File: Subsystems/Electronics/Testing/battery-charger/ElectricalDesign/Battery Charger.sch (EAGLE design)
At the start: 117 parts, among them J1 USB4515-GF-A_REVA, J3 10103592-0001LF, Q1 CSD16406Q3, Q2 CSD16406Q3, Q3 DMN2008LFU, Q4 DMN2008LFU, Q5 DMN2008LFU, Q6 BC817, Q7 BC817, SW6 [Override]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

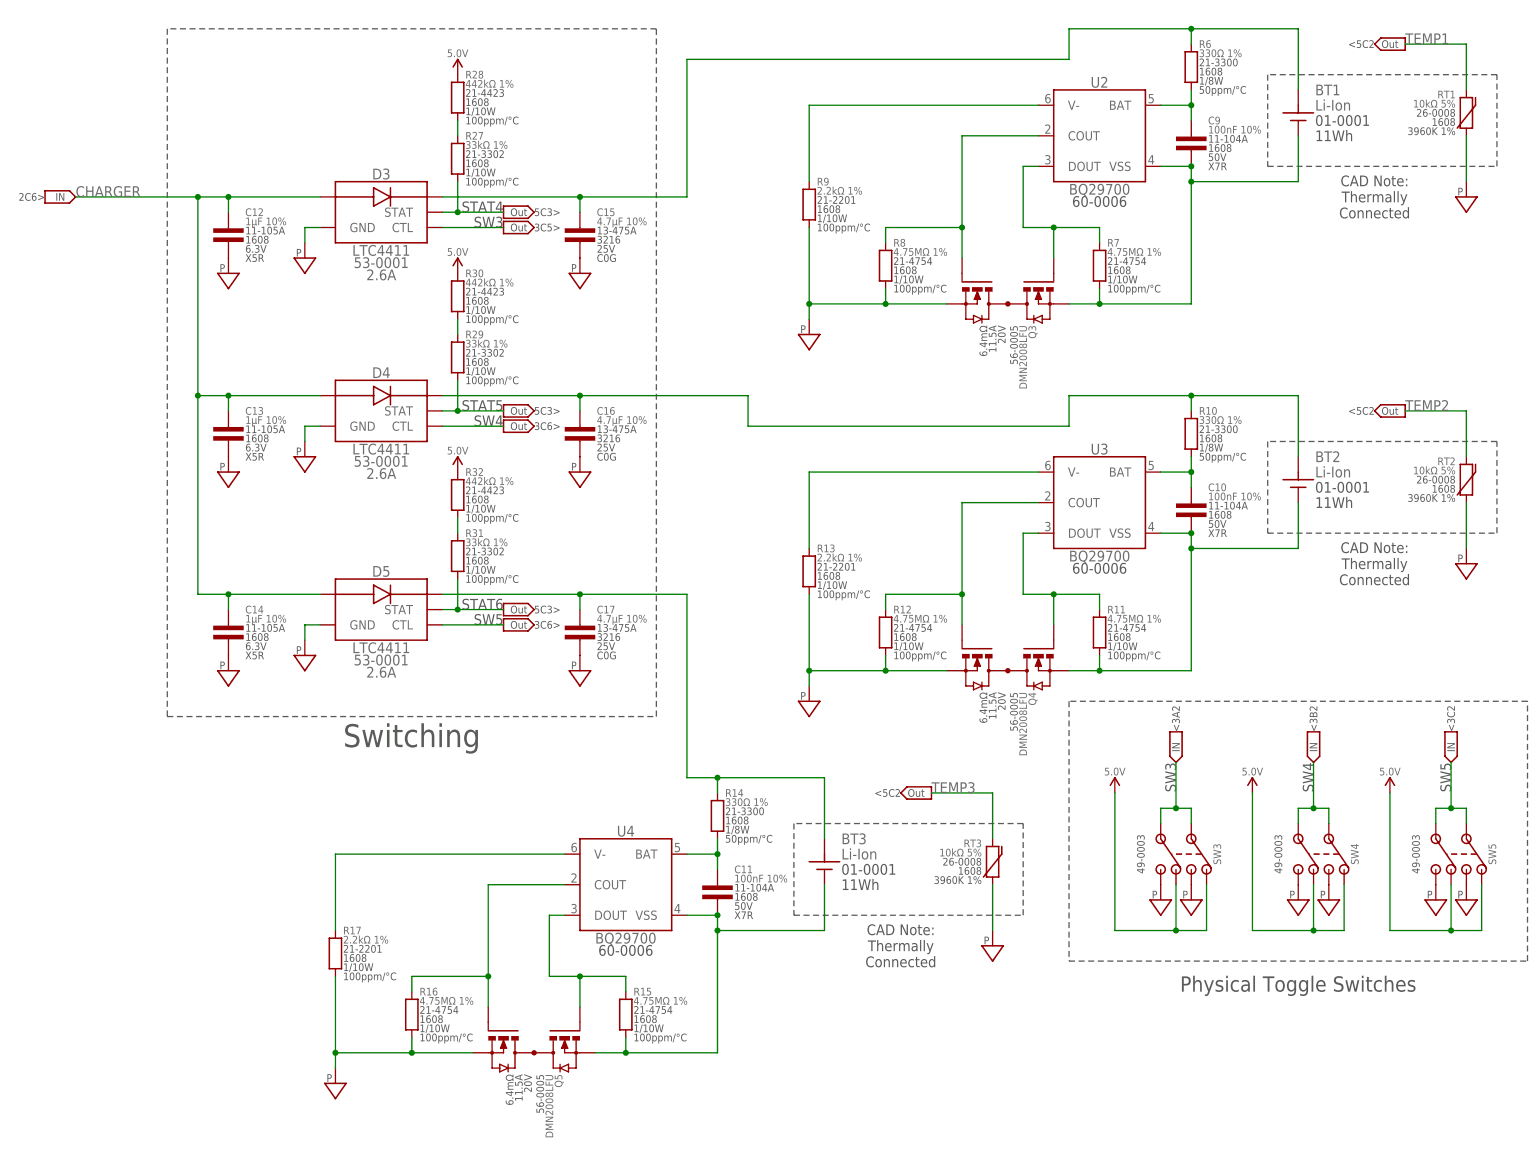
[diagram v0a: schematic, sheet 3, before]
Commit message: Added Test Points
Added test points for the important nets
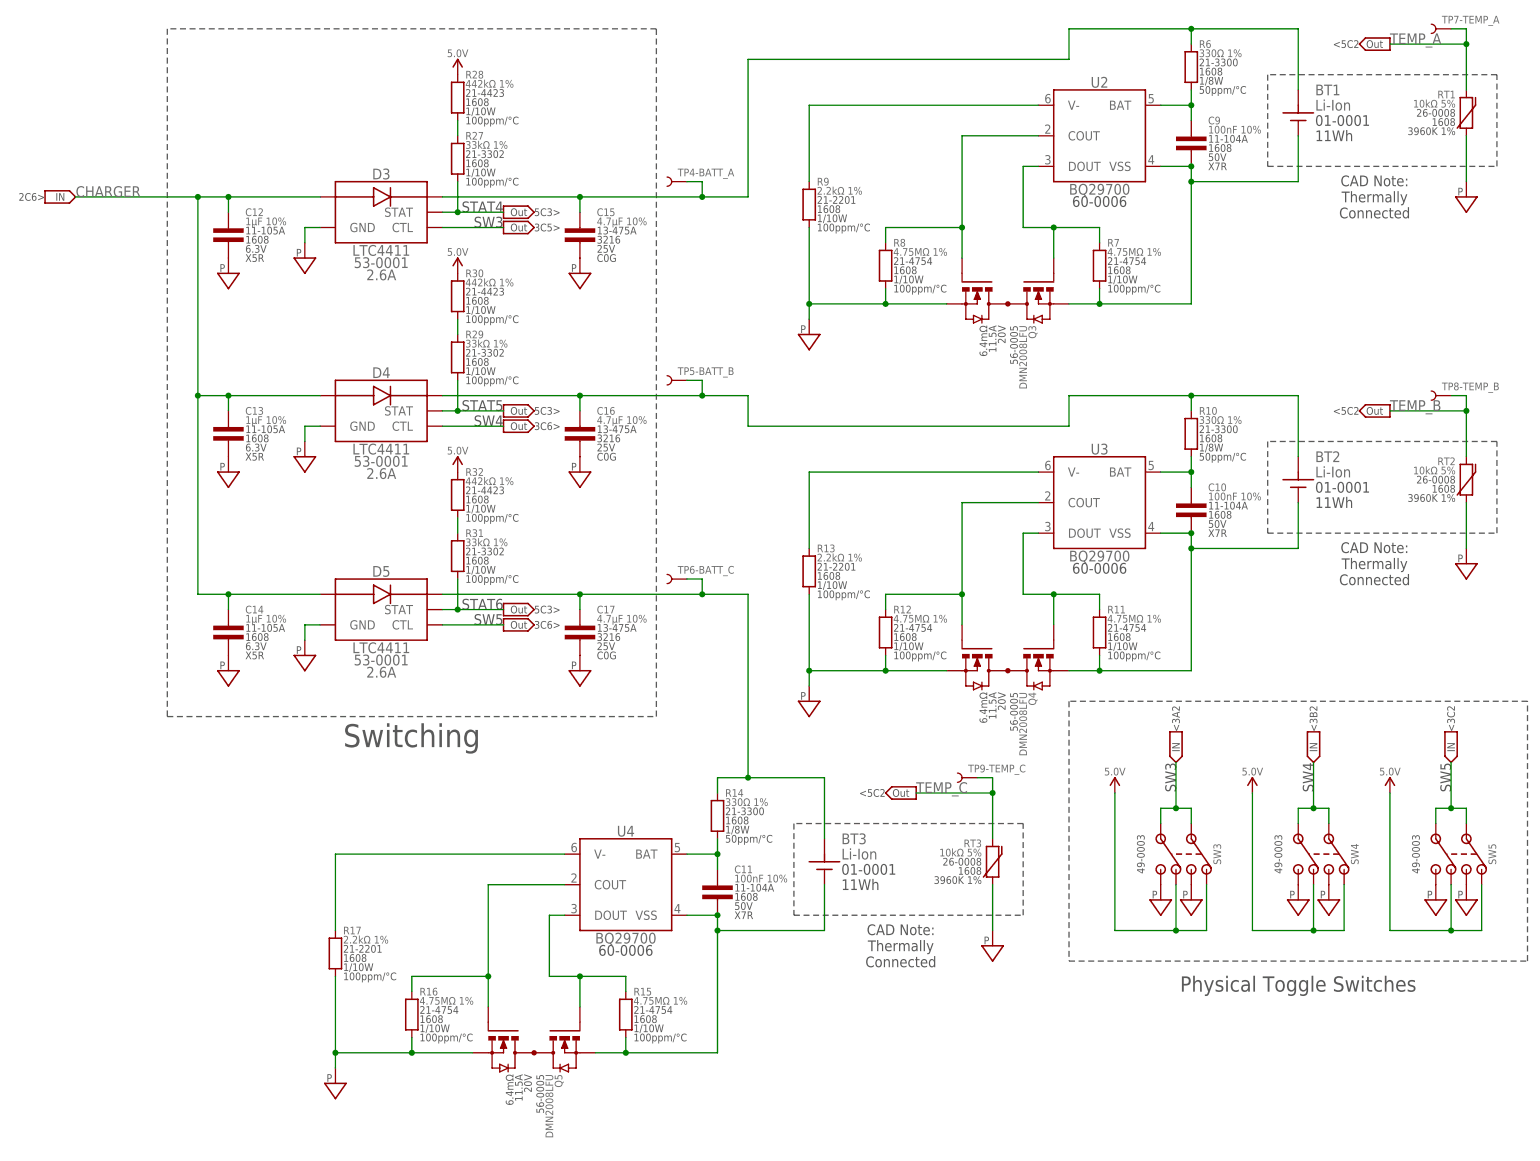
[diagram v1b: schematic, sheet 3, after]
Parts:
- added TP1-5.0V, TP10-USB_5.0V, TP11-CN2102N_VDD, TP12-3.3V, TP2-CHARGER, TP3-TS, TP4-BATT_A, TP5-BATT_B, TP6-BATT_C, TP7-TEMP_A, TP8-TEMP_B, TP9-TEMP_C: TEST_POINT-SMD-C-1.25, CougsInSpace-Connectors:TEST_POINT-SMD-C-1.25
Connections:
- removed net TEMP1: R38.1, RT1.2, U7.IO7
- removed net TEMP2: R39.1, RT2.2, U7.IO8
- removed net TEMP3: R40.1, RT3.2, U7.IO9
- new net TEMP_A: R38.1, RT1.2, TP7-TEMP_A.1, U7.IO7
- new net TEMP_B: R39.1, RT2.2, TP8-TEMP_B.1, U7.IO8
- new net TEMP_C: R40.1, RT3.2, TP9-TEMP_C.1, U7.IO9
- net 3.3V: now also TP12-3.3V.1
- net 5.0V: now also TP1-5.0V.1
- net CHARGER: now also TP2-CHARGER.1
- net CP2102N_VDD: now also TP11-CN2102N_VDD.1
- net D3_OUT: now also TP4-BATT_A.1
- net D4_OUT: now also TP5-BATT_B.1
- net D5_OUT: now also TP6-BATT_C.1
- net TS-ESP: now also TP3-TS.1
- net USB_VDD: now also TP10-USB_5.0V.1
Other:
- moved on the sheet: J3

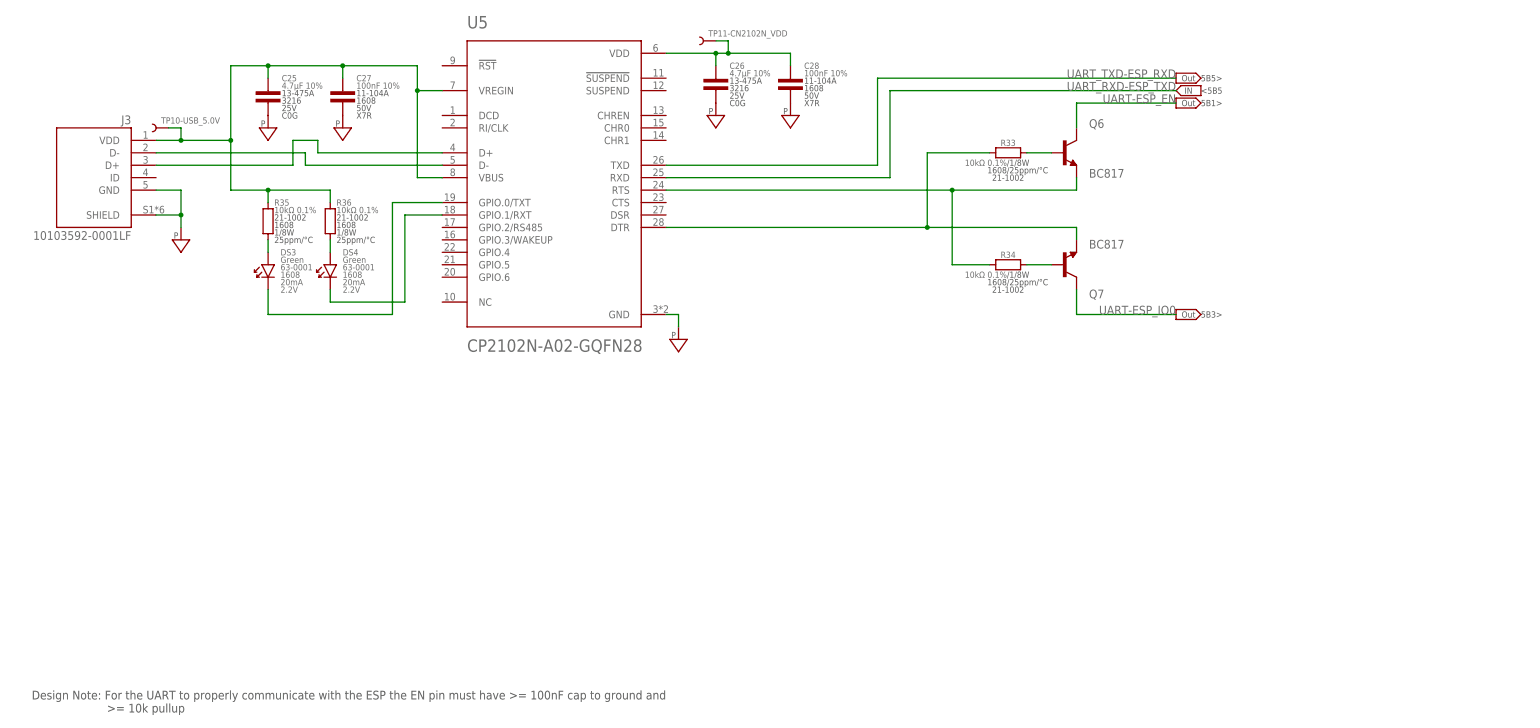
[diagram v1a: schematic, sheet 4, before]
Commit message: Completed Board Layout
Completed board layout, ready for review. Sense resistors were adjusted from 20m to 25m Ohm. Additional sense pins added.
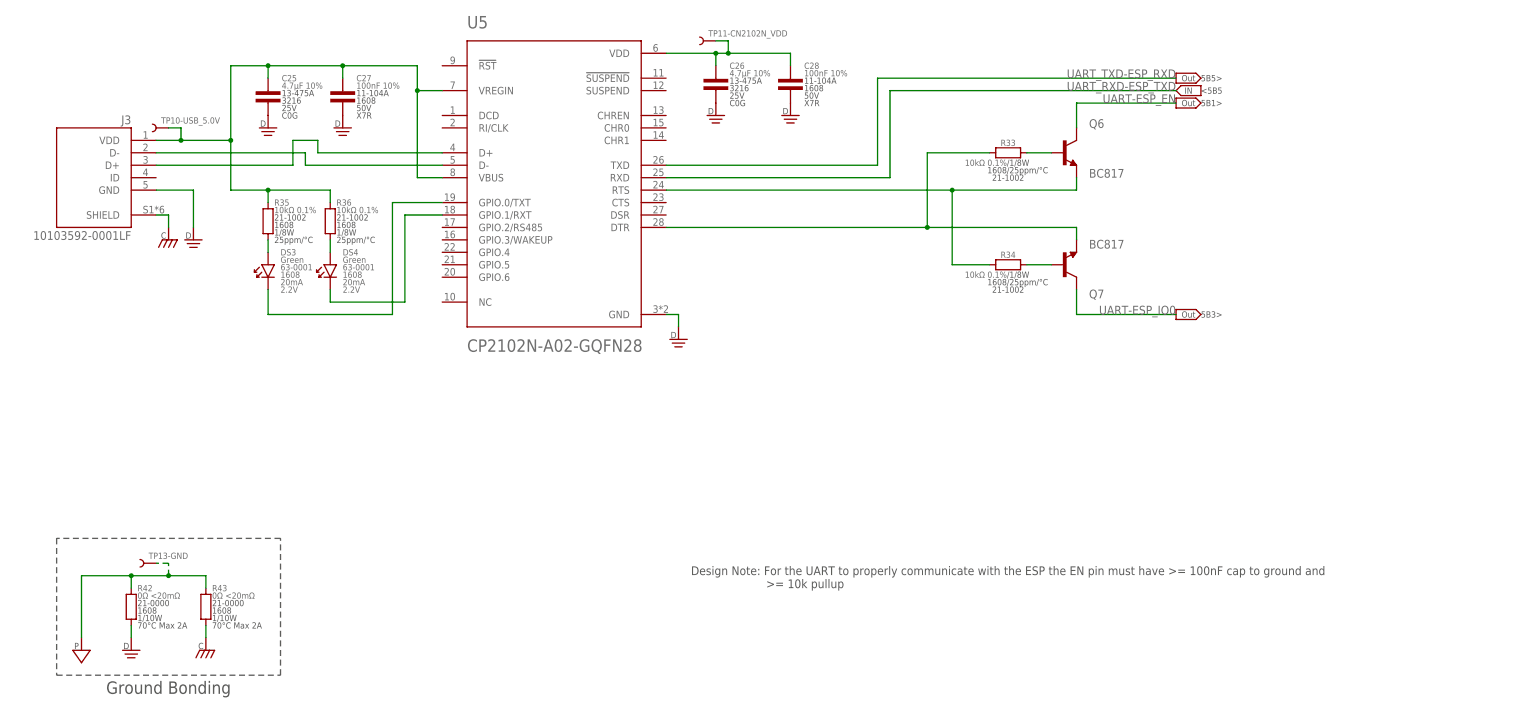
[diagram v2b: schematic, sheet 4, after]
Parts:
- added R42, R43: 0Ω <20mΩ, CougsInSpace-Resistors:RES-V-0-1608
- added TP13-GND, TP14-D1_OUT: TEST_POINT-SMD-C-1.25, CougsInSpace-Connectors:TEST_POINT-SMD-C-1.25
- C20: value 10µF 10% -> 1µF 10%; device CougsInSpace-Capacitors:CAP-V-10UF-1608 -> CougsInSpace-Capacitors:CAP-V-1UF-1608
- JP1: device pinhead:PINHD-1X7 -> pinhead:PINHD-1X11
- R18, R19: value 10mΩ 1% -> 50mΩ 1%; device CougsInSpace-Resistors:RES-H-0.01R-3216 -> CougsInSpace-Resistors:RES-H-0.05R-1608
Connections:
- removed net N$8: R18.2, R19.1
- new net CHASSIS: J1.SHIELD, J3.SHIELD, R43.1
- new net DGND: C25.2, C26.2, C27.2, C28.2, J3.GND, R42.1, U5.GND
- net 3.3V: now also JP1.11
- net 5.0V: now also JP1.1
- net BQ24650_SR_P: now also R19.1
- net CHARGER: now also R18.2
- net D1_OUT: now also TP14-D1_OUT.1
- net ESP32_IO12: now also JP1.9; no longer JP1.7
- net ESP32_IO13: now also JP1.8; no longer JP1.6
- net ESP32_IO14: now also JP1.7; no longer JP1.5
- net ESP32_IO15: now also JP1.6; no longer JP1.4
- net ESP32_IO16: now also JP1.5; no longer JP1.3
- net ESP32_IO17: now also JP1.4; no longer JP1.2
- net ESP32_IO18: now also JP1.3; no longer JP1.1
- net PGND: now also JP1.10, JP1.2, R42.2, R43.2, TP13-GND.1; no longer C25.2, C26.2, C27.2, C28.2, J1.SHIELD, J3.GND, J3.SHIELD, U5.GND
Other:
- note added: "Ground Bonding"
- moved on the sheet: R18, R19

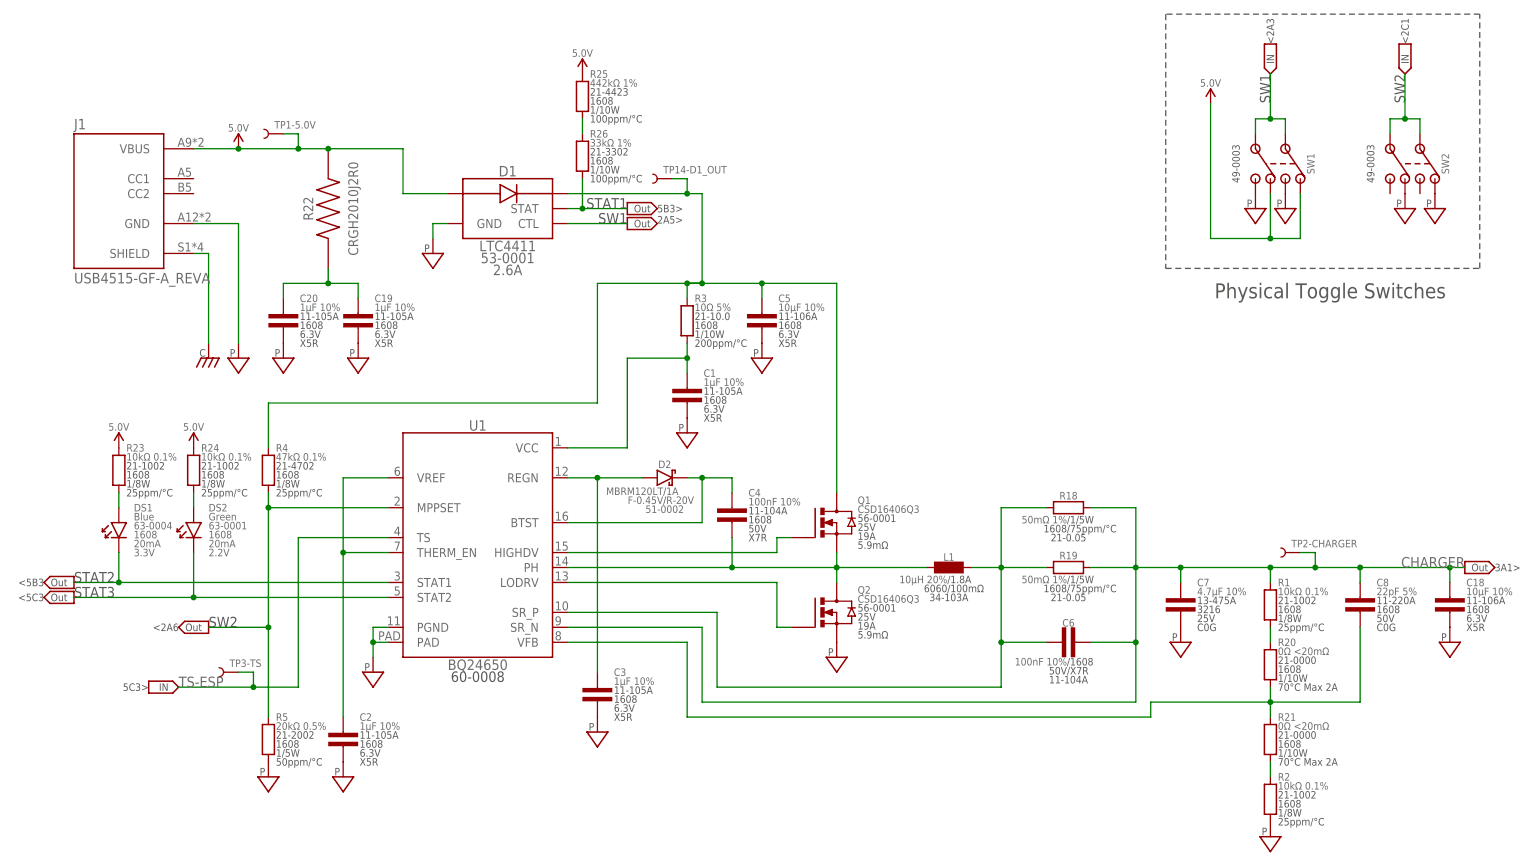
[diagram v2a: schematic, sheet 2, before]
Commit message: Fixed Issues
Fixed some voltage level issues found while writing the documentation
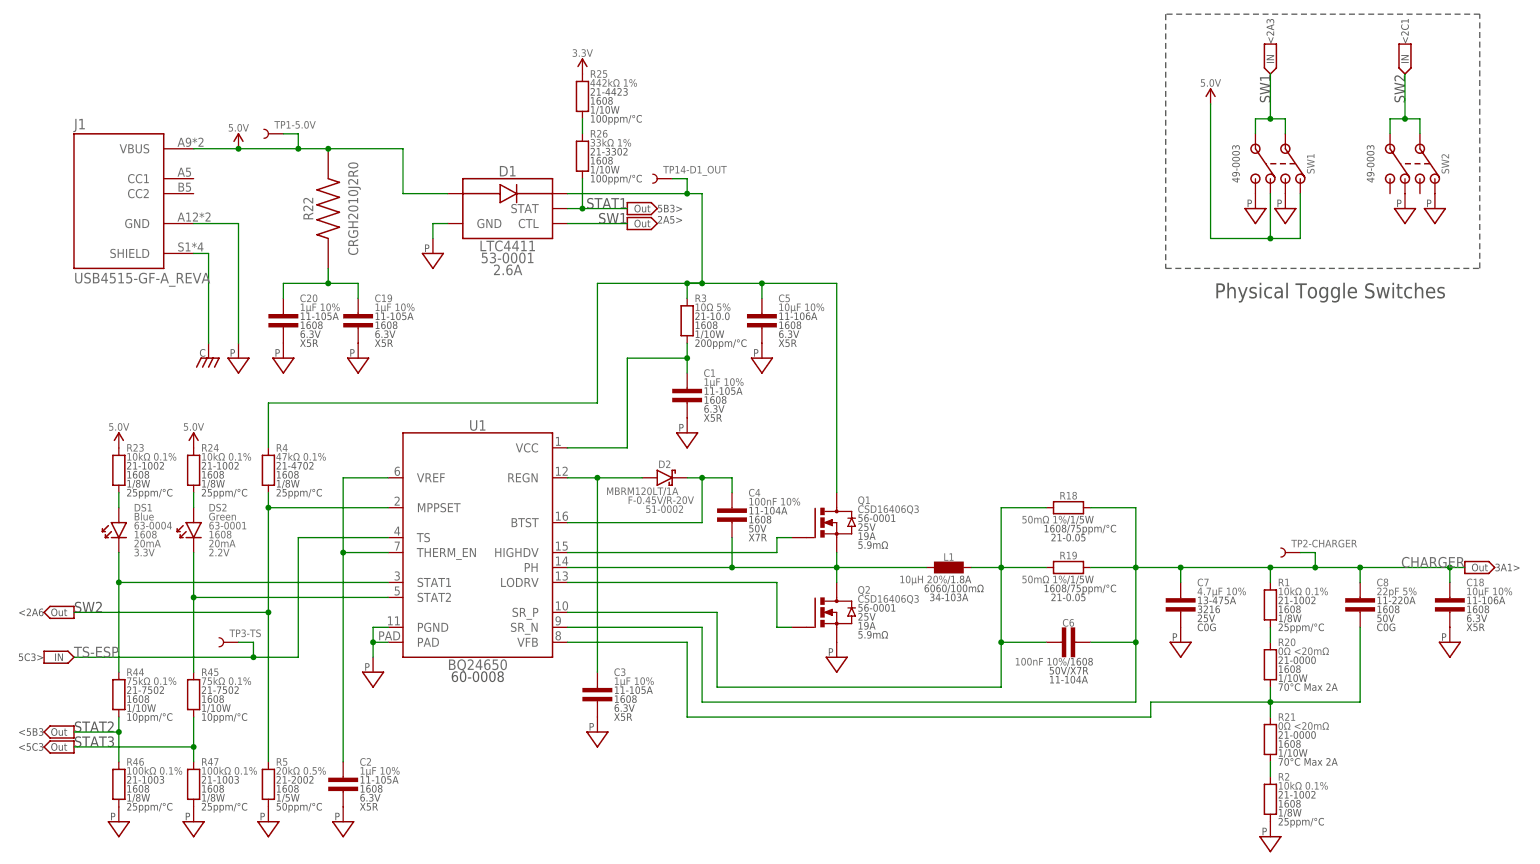
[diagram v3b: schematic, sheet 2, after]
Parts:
- removed R41: 330Ω 1%, CougsInSpace-Resistors:RES-H-330R-1608
- added Q8: DMN53D0L, CougsInSpace-DiscreteSemi:MOSFET-N-SOT23-3
- added R44, R45: 75kΩ 0.1%, CougsInSpace-Resistors:RES-V-75K-1608
- added R46, R47: 100kΩ 0.1%, CougsInSpace-Resistors:RES-V-100K-1608
- added R48, R49: 10kΩ 0.1%, CougsInSpace-Resistors:RES-V-10K-1608
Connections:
- new net BQ24650_STAT1: DS1.C, R44.2, U1.STAT1
- new net BQ24650_STAT2: DS2.C, R45.2, U1.STAT2
- net 3.3V: now also Q8.G, R25.2, R28.2, R30.2, R32.2, R48.2
- net 5.0V: now also R49.2; no longer R25.2, R28.2, R30.2, R32.2
- net LED1_DIN: now also Q8.D, R49.1; no longer R41.2
- net LEDS: now also Q8.S, R48.1; no longer R41.1
- net PGND: now also R46.1, R47.1
- net STAT2: now also R44.1, R46.2; no longer DS1.C, U1.STAT1
- net STAT3: now also R45.1, R47.2; no longer DS2.C, U1.STAT2
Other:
- note added: "External Control Switches"
- note added: "Lighting, Display, and Pin Headers"
- note removed: "Lighting and Display"
- moved on the sheet: C2, R5, TP3-TS
